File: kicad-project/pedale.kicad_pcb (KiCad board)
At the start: 2 copper layers, 121.5 x 81.5 mm, 44 parts, among them IC1 TLV76150DCYR, IC2 TLV76150DCYR, IC3 TLV76150DCYR, IC4 TLV76150DCYR, IC5 TLV76150DCYR

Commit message: modificari 3
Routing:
- net GND: track 34.8 -> 35.6 mm, vias 17 -> 16
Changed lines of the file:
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@@
+	)
+	(segment
+		(start 74.6 65.3)
+		(end 74.6 63)
+		(width 0.5)
+		(layer "F.Cu")
+		(net 4)
 	)
 	(segment
@@
 	)
 	(segment
-		(start 76 65)
-		(end 74.7 63.7)
-		(width 0.5)
-		(layer "F.Cu")
-		(net 4)
-	)
-	(segment
 		(start 64.1 72.4)
 		(end 64.1 70)
@@
 	)
 	(segment
+		(start 74.7 63.7)
+		(end 74.7 63)
+		(width 0.5)
+		(layer "F.Cu")
+		(net 4)
+	)
+	(segment
 		(start 54.6 72.4)
 		(end 54.6 70)
@@
 	)
 	(segment
-		(start 74.7 63.7)
-		(end 74.7 63)
+		(start 74.5 63.9)
+		(end 74.7 63.7)
 		(width 0.5)
 		(layer "F.Cu")
@@
 	)
 	(via
-		(at 76 65)
-		(size 0.6)
-		(drill 0.3)
-		(layers "F.Cu" "B.Cu")
-		(free yes)
-		(net 4)
-	)
-	(via
-		(at 44.1 72.4)
+		(at 74.6 65.3)
 		(size 0.6)
 		(drill 0.3)
@@
 	)
 	(segment
+		(start 32.5 38.5)
+		(end 26.325 38.5)
+		(width 0.35)
+		(layer "B.Cu")
+		(net 119)
+	)
+	(segment
 		(start 37.5 43.5)
 		(end 32.5 38.5)
-		(width 0.25)
-		(layer "B.Cu")
-		(net 119)
-	)
-	(segment
-		(start 32.5 38.5)
-		(end 26.325 38.5)
-		(width 0.25)
+		(width 0.35)
 		(layer "B.Cu")
 		(net 119)
@@
 		(start 107 43.5)
 		(end 37.5 43.5)
-		(width 0.25)
+		(width 0.35)
 		(layer "B.Cu")
 		(net 119)
@@
 		(start 39.5 52)
 		(end 34.5 47)
-		(width 0.25)
+		(width 0.35)
 		(layer "B.Cu")
 		(net 120)
@@
 		(start 34.5 47)
 		(end 26.325 47)
-		(width 0.25)
+		(width 0.35)
 		(layer "B.Cu")
 		(net 120)
@@
 		(start 107 52)
 		(end 39.5 52)
-		(width 0.25)
+		(width 0.35)
 		(layer "B.Cu")
 		(net 120)
@@
 	)
 	(segment
+		(start 107 60.5)
+		(end 41.5 60.5)
+		(width 0.35)
+		(layer "B.Cu")
+		(net 121)
+	)
+	(segment
 		(start 36.25 55.25)
 		(end 26.325 55.25)
-		(width 0.25)
-		(layer "B.Cu")
-		(net 121)
-	)
-	(segment
-		(start 107 60.5)
-		(end 41.5 60.5)
-		(width 0.25)
+		(width 0.35)
 		(layer "B.Cu")
 		(net 121)
@@
 		(start 41.5 60.5)
 		(end 36.25 55.25)
-		(width 0.25)
+		(width 0.35)
 		(layer "B.Cu")
 		(net 121)
@@
 	)
 	(segment
+		(start 34.5 76)
+		(end 26.825 76)
+		(width 0.35)
+		(layer "B.Cu")
+		(net 122)
+	)
+	(segment
 		(start 41.5 69)
 		(end 34.5 76)
-		(width 0.25)
+		(width 0.35)
 		(layer "B.Cu")
 		(net 122)
@@
 		(start 107 69)
 		(end 41.5 69)
-		(width 0.25)
-		(layer "B.Cu")
-		(net 122)
-	)
-	(segment
-		(start 34.5 76)
-		(end 26.825 76)
-		(width 0.25)
+		(width 0.35)
 		(layer "B.Cu")
 		(net 122)
@@
 	)
 	(segment
+		(start 41.5 75)
+		(end 32.5 84)
+		(width 0.35)
+		(layer "B.Cu")
+		(net 123)
+	)
+	(segment
+		(start 32.5 84)
+		(end 26.825 84)
+		(width 0.35)
+		(layer "B.Cu")
+		(net 123)
+	)
+	(segment
 		(start 102.5 75)
 		(end 41.5 75)
-		(width 0.25)
+		(width 0.35)
 		(layer "B.Cu")
 		(net 123)
-	)
-	(segment
-		(start 41.5 75)
-		(end 32.5 84)
-		(width 0.25)
-		(layer "B.Cu")
-		(net 123)
-	)
-	(segment
-		(start 32.5 84)
-		(end 26.825 84)
-		(width 0.25)
-		(layer "B.Cu")
-		(net 123)

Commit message: modificari 4
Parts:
- moved U6 0.50 mm to (26.3, 76.0)
- moved U7 0.50 mm to (26.3, 84.0)
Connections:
- J1 pad 11: GND -> unconnected-(J1-pte24-Pad11)
- J1 pad 12: unconnected-(J1-pte24-Pad12) -> GND
- J13 pad 15: unconnected-(J13-ptc31-Pad15) -> 12V
- J13 pad 16: 12V -> unconnected-(J13-ptc31-Pad16)
- J14 pad 1: unconnected-(J14-ptc19-Pad1) -> Net-(J14-ptd1)
- J14 pad 10: Net-(J14-pta9) -> unconnected-(J14-ptc12-Pad10)
- J14 pad 2: Net-(J14-ptd1) -> unconnected-(J14-ptc19-Pad2)
- J14 pad 3: unconnected-(J14-ptc18-Pad3) -> Net-(J14-ptd0)
- J14 pad 4: Net-(J14-ptd0) -> unconnected-(J14-ptc18-Pad4)
- J14 pad 5: unconnected-(J14-ptb29-Pad5) -> Net-(J14-pta13)
- J14 pad 6: Net-(J14-pta13) -> unconnected-(J14-ptb29-Pad6)
- J14 pad 7: unconnected-(J14-ptb2-Pad7) -> Net-(J14-pta8)
- J14 pad 8: Net-(J14-pta8) -> unconnected-(J14-ptb2-Pad8)
- J14 pad 9: unconnected-(J14-ptc12-Pad9) -> Net-(J14-pta9)
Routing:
- net Net-(J14-pta8): track 35.8 -> 32.1 mm
- net Net-(J14-ptd1): track 51.6 -> 48.1 mm
- net Net-(J14-ptd0): track 43.6 -> 40.1 mm
- net Net-(J14-pta13): track 36.6 -> 33.1 mm
- net Net-(J14-pta9): track 34.4 -> 31.9 mm
- net 12V: track 84.5 -> 83.9 mm

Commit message: viorel checked
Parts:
- added D1: SS32, Diode_SMD:D_SMB, F.Cu at (129.0, 54.0)
- added H1: MountingHole_Pad, MountingHole:MountingHole_3.2mm_M3_DIN965_Pad, F.Cu at (23.0, 94.0)
- added H2: MountingHole_Pad, MountingHole:MountingHole_3.2mm_M3_DIN965_Pad, F.Cu at (133.0, 94.0)
- added H3: MountingHole_Pad, MountingHole:MountingHole_3.2mm_M3_DIN965_Pad, F.Cu at (133.0, 29.0)
- added H4: MountingHole_Pad, MountingHole:MountingHole_3.2mm_M3_DIN965_Pad, F.Cu at (23.0, 29.0)
- added H5: MountingHole_Pad, MountingHole:MountingHole_3.2mm_M3_DIN965_Pad, F.Cu at (125.2, 29.5)
- added H6: MountingHole_Pad, MountingHole:MountingHole_3.2mm_M3_DIN965_Pad, F.Cu at (31.6, 29.5)
- added H7: MountingHole_Pad, MountingHole:MountingHole_3.2mm_M3_DIN965_Pad, F.Cu at (31.6, 93.2)
- added H8: MountingHole_Pad, MountingHole:MountingHole_3.2mm_M3_DIN965_Pad, F.Cu at (125.3, 93.3)
- U1, U8: footprint Connector_PinSocket_2.00mm:PinSocket_1x02_P2.00mm_Horizontal -> Connector_JST:JST_PH_B2B-PH-K_1x02_P2.00mm_Vertical
- U2, U3, U5, U6, U7: footprint Connector_PinSocket_2.00mm:PinSocket_1x03_P2.00mm_Horizontal -> Connector_JST:JST_PH_B3B-PH-K_1x03_P2.00mm_Vertical
- moved R13 51.7 mm to (35.6, 42.5), turned to 0 degrees
- moved R14 45.1 mm to (43.8, 42.5)
- moved R10 41.5 mm to (35.5, 49.8), turned to 0 degrees
- moved R12 40.8 mm to (51.8, 42.5), turned to 0 degrees
- moved R11 34.4 mm to (43.0, 49.8)
- moved R1 33.8 mm to (33.0, 86.0), turned to 90 degrees
- moved R4 32.1 mm to (35.9, 79.2), turned to 0 degrees
- moved R7 31.3 mm to (35.4, 58.5), turned to 0 degrees
- moved R9 29.6 mm to (50.5, 49.8), turned to 0 degrees
- moved R2 25.6 mm to (37.5, 86.0), turned to -90 degrees
- moved R8 24.1 mm to (42.6, 58.5)
- moved R5 22.1 mm to (43.1, 79.2)
- moved R6 20.2 mm to (49.9, 58.5), turned to 0 degrees
- moved R0 16.6 mm to (42.0, 86.0), turned to 90 degrees
- moved R3 11.4 mm to (50.4, 79.2), turned to 0 degrees
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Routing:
- net Net-(U3-A0): track 68.6 -> 7.41 mm
- net Net-(U6-A0): track 65.5 -> 7.90 mm
- net Net-(U2-A0): track 59.7 -> 7.29 mm
- net Net-(U5-A0): track 58.7 -> 7.58 mm
- net Net-(U7-A0): track 58.3 -> 7.25 mm
- net Net-(J14-pta9): track 31.9 -> 81.7 mm
- net Net-(J14-pta8): track 32.1 -> 72.3 mm
- net Net-(J14-pta13): track 33.1 -> 59.5 mm
- net GND: track 35.6 -> 22.8 mm, vias 16 -> 12
- net Net-(J14-ptd0): track 40.1 -> 48.2 mm
- net Net-(R7-Pad2): track 7.00 -> 2.45 mm
- net Net-(R4-Pad2): track 7.00 -> 2.45 mm
- net Net-(R10-Pad2): track 7.00 -> 2.70 mm
- net Net-(R13-Pad2): track 7.00 -> 3.30 mm
- net Net-(J14-ptd1): track 48.1 -> 44.4 mm
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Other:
- board size 121.5 x 81.5 mm -> 118 x 73 mm

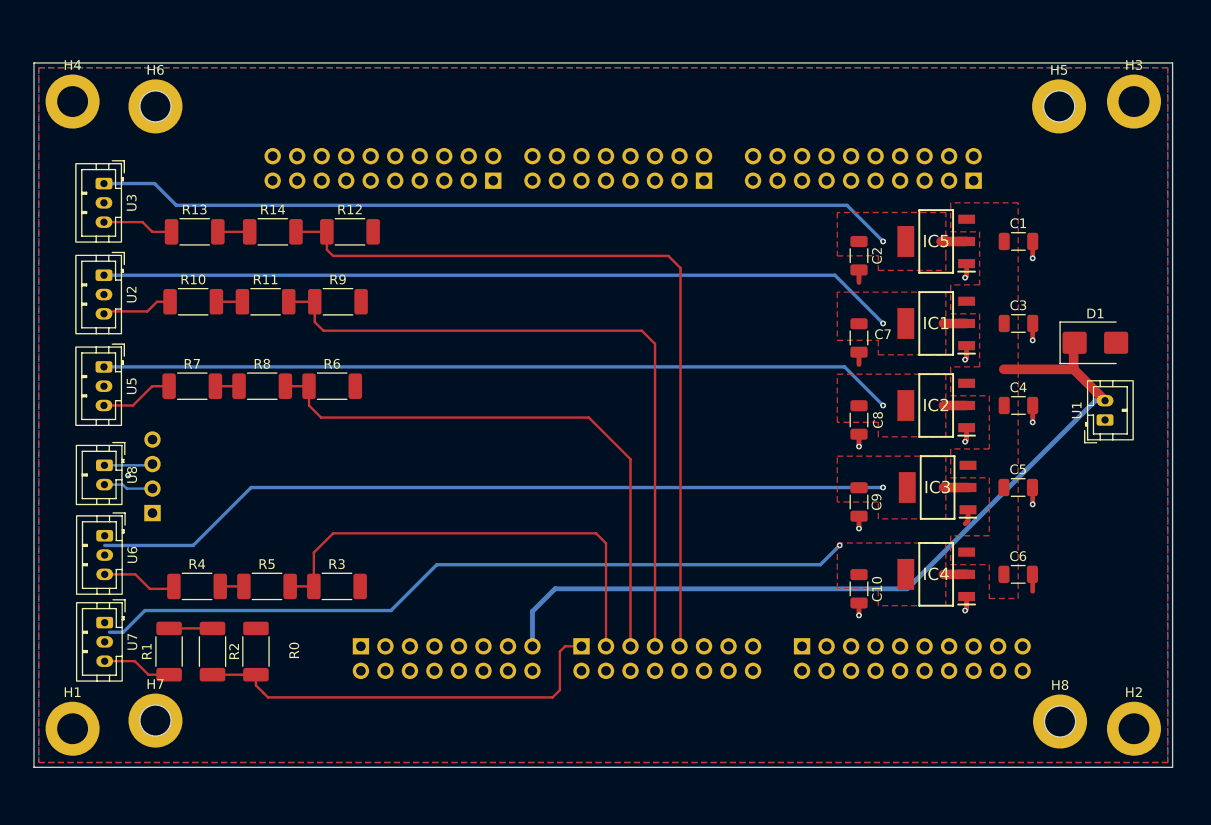
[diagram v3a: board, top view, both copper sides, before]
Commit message: CAN_IN + CAN_OUT - added
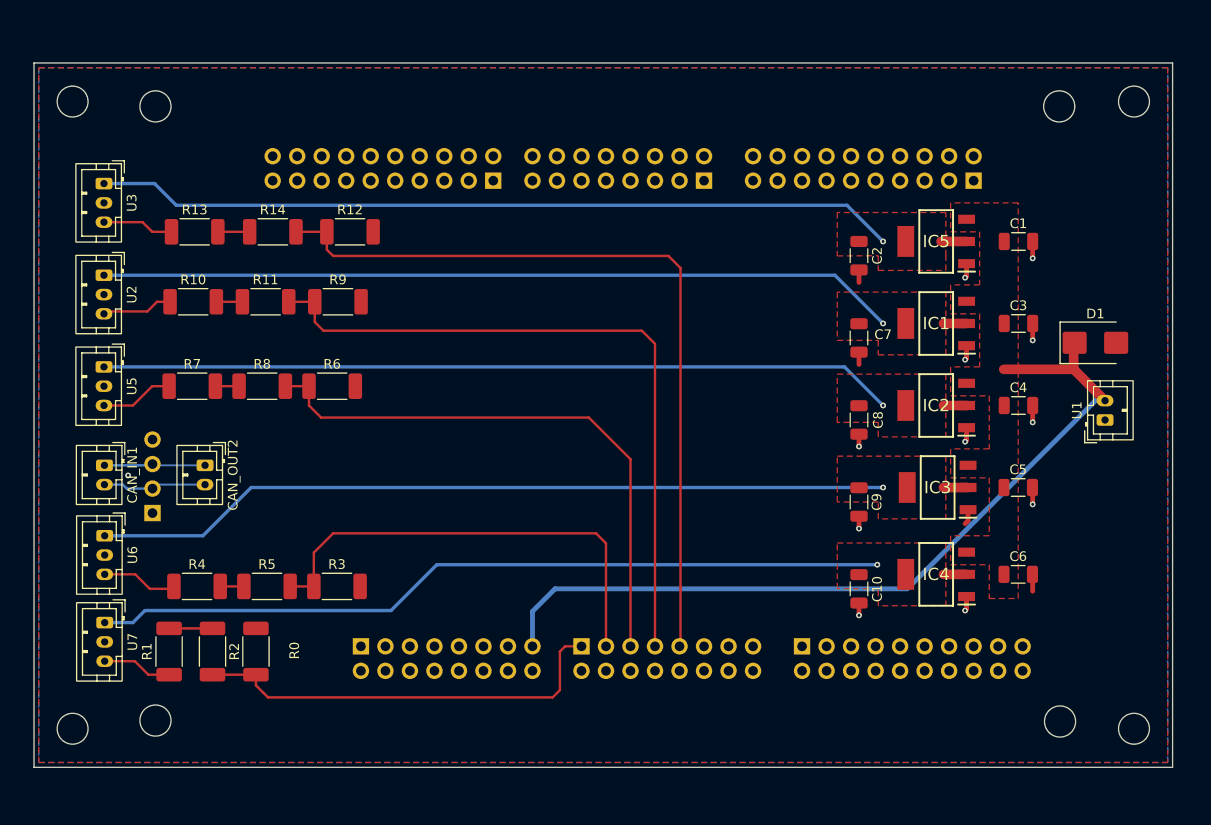
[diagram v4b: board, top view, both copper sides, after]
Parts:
- removed H1, H2, H3, H4, H5, H6, H7, H8: MountingHole_Pad, MountingHole:MountingHole_3.2mm_M3_DIN965_Pad
- added CAN_OUT2: ~, Connector_JST:JST_PH_B2B-PH-K_1x02_P2.00mm_Vertical, F.Cu at (36.7, 66.7)
- renumbered U8 to CAN_IN1
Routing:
- net /CAN_N: track 5.46 -> 11.1 mm
- net /CAN_P: track 5.03 -> 10.5 mm
- net /5V_5: track 81.8 -> 85.0 mm
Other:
- outline, holes or cut-outs redrawn

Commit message: V_divirders removed+ Connectors moved
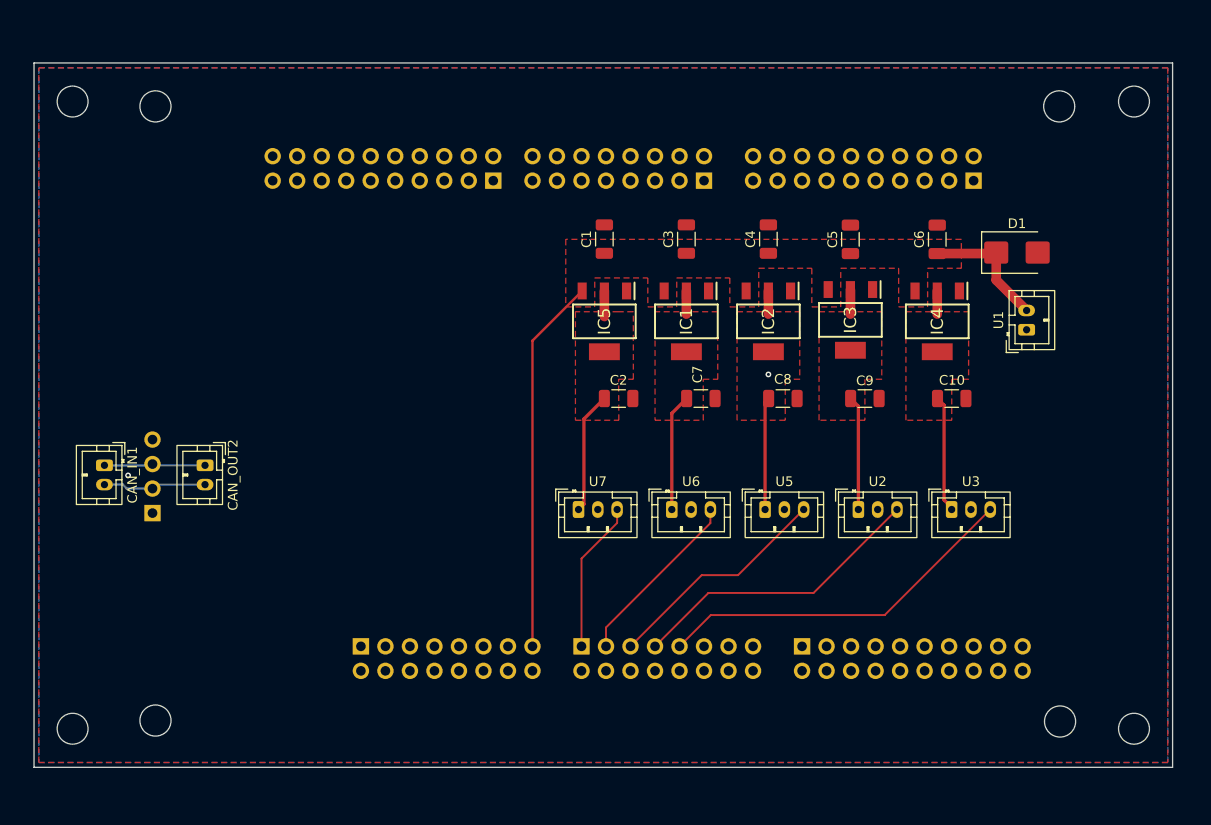
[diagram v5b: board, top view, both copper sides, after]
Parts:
- removed R0, R12, R3, R6, R9: R4.7k, Resistor_SMD:R_2010_5025Metric_Pad1.40x2.65mm_HandSolder
- removed R1, R10, R13, R4, R7: R2.2k, Resistor_SMD:R_2010_5025Metric_Pad1.40x2.65mm_HandSolder
- removed R11, R14, R2, R5, R8: R220, Resistor_SMD:R_2010_5025Metric_Pad1.40x2.65mm_HandSolder
- moved U3 94.1 mm to (114.1, 71.3), turned to 0 degrees
- moved U2 81.9 mm to (104.4, 71.3), turned to 0 degrees
- moved U5 70.1 mm to (94.8, 71.3), turned to 0 degrees
- moved U6 58.8 mm to (85.1, 71.3), turned to 0 degrees
- moved U7 50.5 mm to (75.4, 71.3), turned to 0 degrees
- moved C1 42.9 mm to (78.1, 43.3), turned to 90 degrees
- moved C6 35.7 mm to (112.6, 43.3), turned to 90 degrees
- moved C3 35.5 mm to (86.6, 43.3), turned to 90 degrees
- moved IC5 35.4 mm to (78.1, 51.8), turned to -90 degrees
- moved C4 31.1 mm to (95.1, 43.3), turned to 90 degrees
- moved C5 31.0 mm to (103.6, 43.3), turned to 90 degrees
- moved C2 29.0 mm to (79.6, 59.8), turned to 0 degrees
- moved IC4 26.2 mm to (112.6, 51.8), turned to -90 degrees
- moved IC1 25.9 mm to (86.6, 51.8), turned to -90 degrees
- moved C10 21.9 mm to (114.1, 59.8), turned to 0 degrees
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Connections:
- C10 pad 1: /5V_5 -> /5V_1
- C2 pad 1: /5V_1 -> /5V_5
- C7 pad 1: /5V_2 -> /5V_4
- C9 pad 1: /5V_4 -> /5V_2
- IC1 pad 2: /5V_2 -> /5V_4
- IC1 pad 4: /5V_2 -> /5V_4
- IC3 pad 2: /5V_4 -> /5V_2
- IC3 pad 4: /5V_4 -> /5V_2
- IC4 pad 2: /5V_5 -> /5V_1
- IC4 pad 4: /5V_5 -> /5V_1
- IC5 pad 2: /5V_1 -> /5V_5
- IC5 pad 4: /5V_1 -> /5V_5
- U2 pad 3: Net-(U2-A0) -> Net-(J14-pta8)
- U3 pad 3: Net-(U3-A0) -> Net-(J14-pta9)
- U5 pad 3: Net-(U5-A0) -> Net-(J14-pta13)
- U6 pad 3: Net-(U6-A0) -> Net-(J14-ptd0)
- U7 pad 3: Net-(U7-A0) -> Net-(J14-ptd1)
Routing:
- net /5V_1: track 85.9 -> 14.5 mm, vias 1 -> 0
- net /5V_2: track 85.1 -> 14.4 mm, vias 1 -> 0
- net /5V_4: track 85.3 -> 14.5 mm, vias 1 -> 0
- net /5V_3: track 84.8 -> 14.1 mm
- net /5V_5: track 85.0 -> 15.3 mm, vias 1 -> 0
- net Net-(J14-pta9): track 81.7 -> 38.1 mm
- net Net-(J14-pta8): track 72.3 -> 30.9 mm
- net Net-(J14-pta13): track 59.5 -> 23.8 mm
- net 12V: track 86.6 -> 52.4 mm
- net Net-(J14-ptd0): track 48.2 -> 18.7 mm
- net Net-(J14-ptd1): track 44.4 -> 15.7 mm
- net GND: track 22.8 -> 0.07 mm, vias 12 -> 1
- net Net-(U6-A0): track 7.90 -> 0.00 mm
- net Net-(U5-A0): track 7.58 -> 0.00 mm
- net Net-(U3-A0): track 7.41 -> 0.00 mm
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
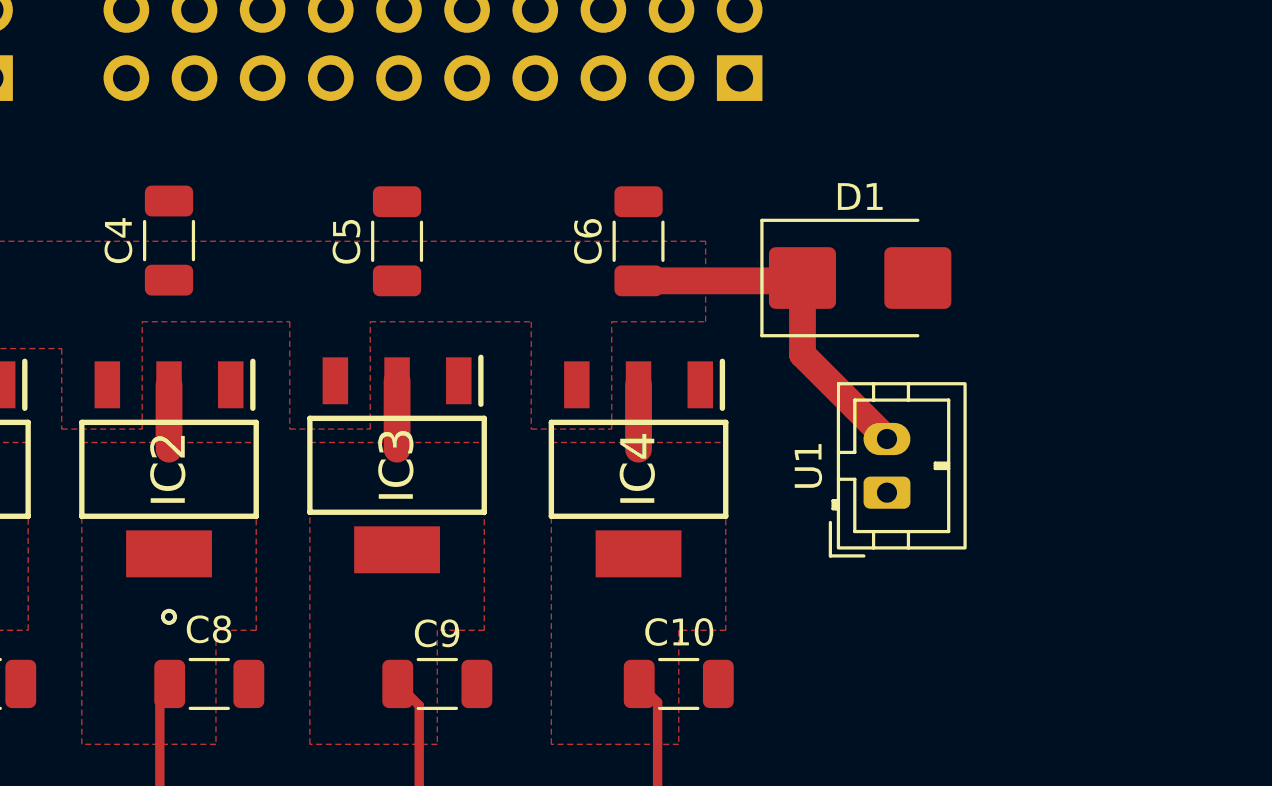
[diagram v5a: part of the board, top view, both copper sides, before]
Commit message: GND on Diode placed
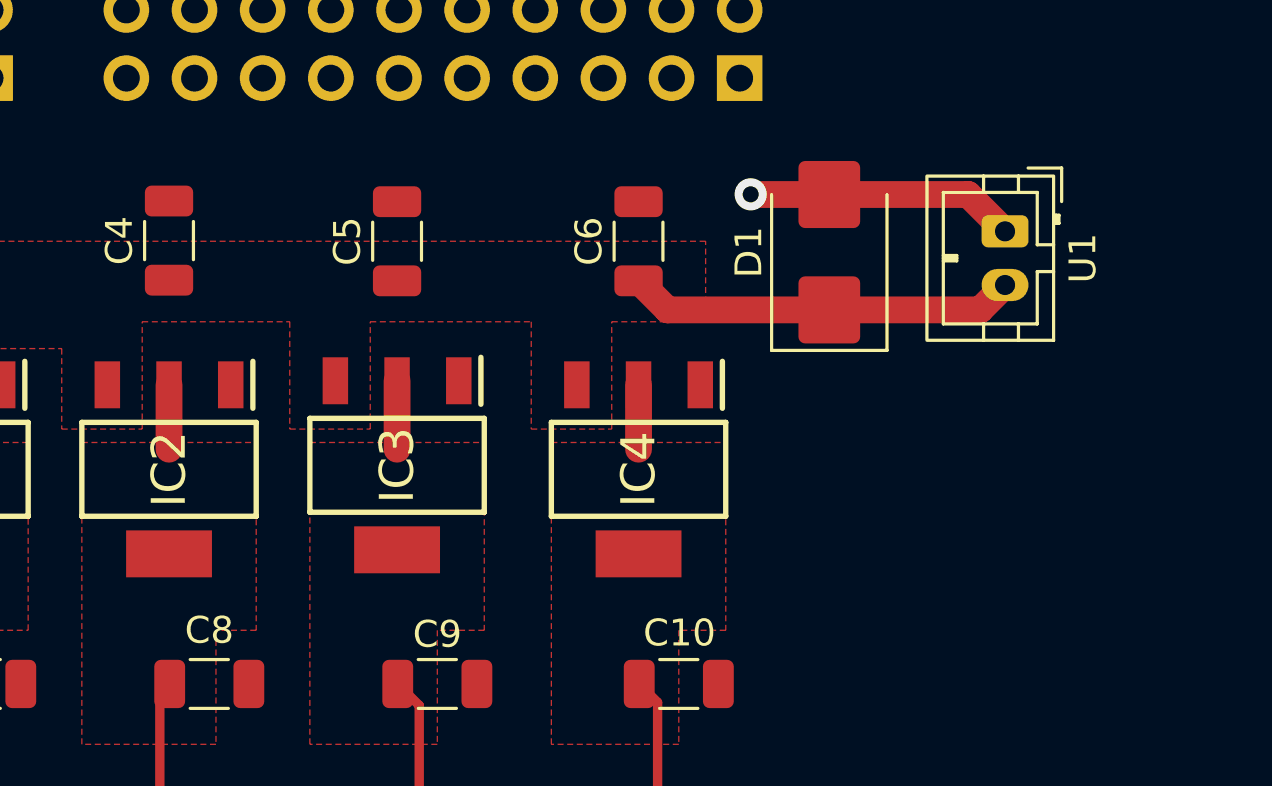
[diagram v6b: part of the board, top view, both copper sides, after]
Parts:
- moved U1 10.7 mm to (126.3, 42.9), turned to -90 degrees
- moved D1 1.50 mm to (119.7, 43.7), turned to 90 degrees
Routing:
- net GND: track 0.07 -> 10.1 mm, vias 1 -> 2
- net 12V: track 52.4 -> 53.5 mm
- net /5V_3: vias 1 -> 0
